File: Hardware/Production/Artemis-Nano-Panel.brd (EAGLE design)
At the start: 120.7 x 75.7 mm, 768 parts, among them J10 USB-C, J11 CORTEX_DEBUG, J21 USB-C, J22 CORTEX_DEBUG, J32 USB-C, J33 CORTEX_DEBUG, J43 USB-C, J44 CORTEX_DEBUG, J54 USB-C, J55 CORTEX_DEBUG, J65 USB-C, J66 CORTEX_DEBUG, U1 MCP73831, U10 3.3V, U11 ARTEMIS_MODULESMD, U12 CH340E_MSOP10, U13 MCP73831, U14 3.3V, U15 ARTEMIS_MODULESMD, U16 CH340E_MSOP10, U17 MCP73831, U18 3.3V, U19 ARTEMIS_MODULESMD, U2 MCP73831, U20 CH340E_MSOP10, U21 MCP73831, U22 3.3V, U23 ARTEMIS_MODULESMD, U24 CH340E_MSOP10, U3 3.3V, U4 ARTEMIS_MODULESMD, U5 3.3V, U6 CH340E_MSOP10, U7 ARTEMIS_MODULESMD, U8 CH340E_MSOP10, U9 MCP73831, Y1 32.768kHz, Y2 32.768kHz, Y3 32.768kHz, Y4 32.768kHz, Y5 32.768kHz, Y6 32.768kHz

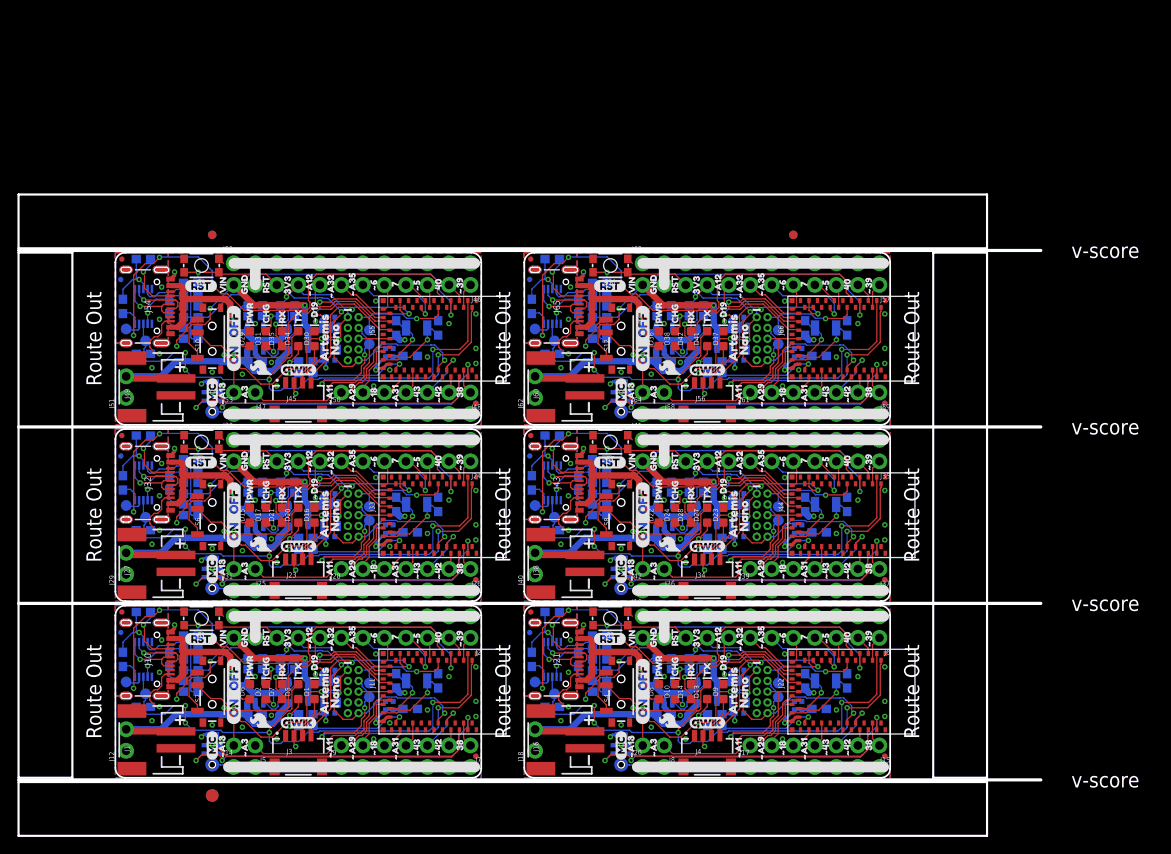
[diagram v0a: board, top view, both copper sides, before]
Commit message: Fixed TX/RX LED label swap
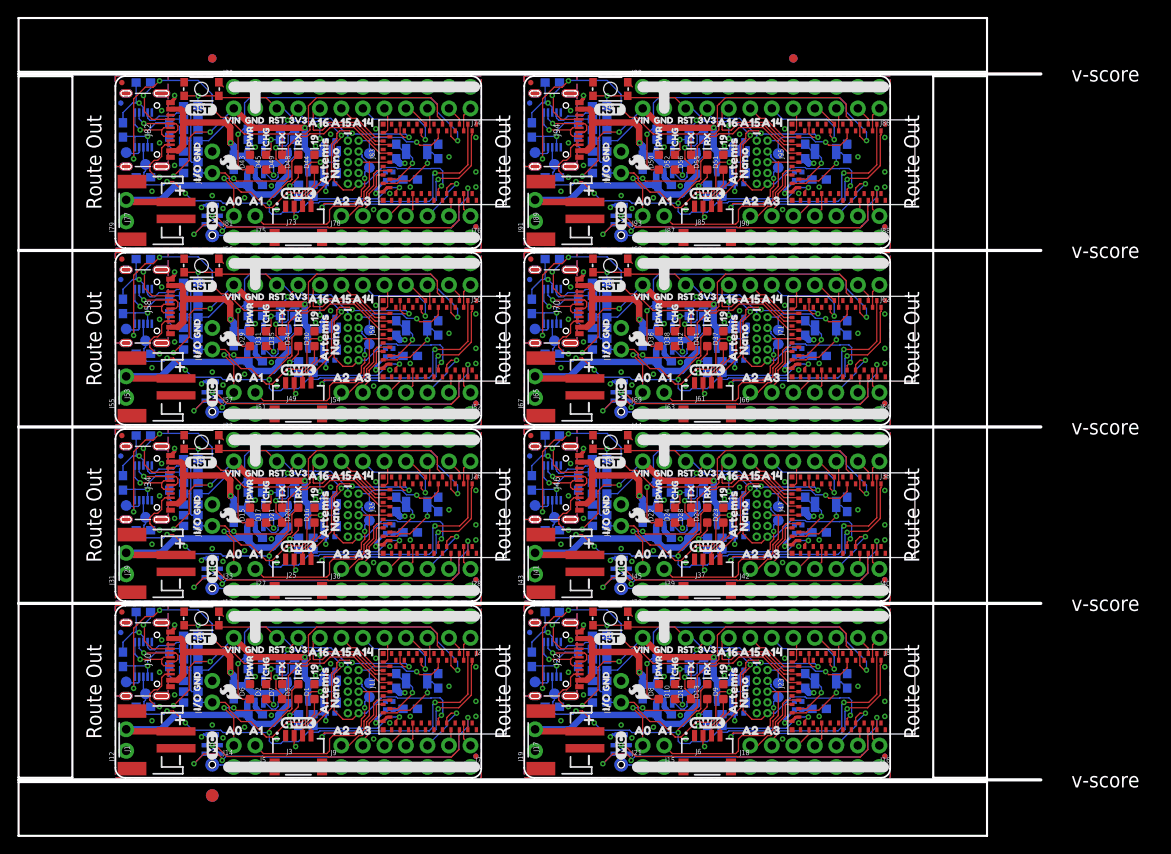
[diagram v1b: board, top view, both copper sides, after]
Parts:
- removed S10, S12: (no value), SparkFun-Switches:SWITCH_SPST_SMD_A
- removed S11, S9: RESET, SparkFun-Switches:TACTILE_SWITCH_SMD_4.6X2.8MM
- added C100, C113, C115, C98: 0.1uF, SparkFun-Capacitors:0603
- added C101, C116: 2.2uF, SparkFun-Capacitors:0603
- added C102, C117: 10uF, SparkFun-Capacitors:0603
- added C103, C108, C109, C118, C93, C94: 1.0uF, SparkFun-Capacitors:0402-TIGHT
- added C104, C119: 1nF, SparkFun-Capacitors:0603
- added C105, C114, C120, C99: 0.1uF, SparkFun-Capacitors:0402-TIGHT
- added C106, C107, C91, C92: 4.7uF, SparkFun-Capacitors:0603
- added C110, C111, C95, C96: 15pF, SparkFun-Capacitors:0603
- added C112, C97: 10nF, SparkFun-Capacitors:0603
- added D43, D50: RED, SparkFun-LED:LED-0603
- added D44, D51: BLUE, SparkFun-LED:LED-0603
- added D45, D48, D52, D55: Yellow, SparkFun-LED:LED-0603
- added D46, D47, D53, D54: 1A/23V/620mV, SparkFun-DiscreteSemi:SOD-323
- added D49, D56: GREEN, SparkFun-LED:LED-0603
- added E7, E8: SPH0641LM4H, SparkFun-Sensors:SPH0641LM4H-1_MICROPHONE
- added FD25, FD26, FD27, FD28, FD29, FD30, FD31, FD32: FIDUCIALUFIDUCIAL, SparkFun-Aesthetics:FIDUCIAL-MICRO
- added FRAME7, FRAME8: FRAME-LETTERNO_PACKAGE, SparkFun-Aesthetics:DUMMY
- added J67, J69, J72, J75, J79, J81, J84, J87, J91, J93, J96: (no value), SparkFun-Connectors:1X02_NO_SILK
- added J68, J74, J80, J86, J92: (no value), SparkFun-Connectors:1X12_NO_SILK
- added J70, J82, J94: USB-C, SparkFun-Connectors:USB-C-16P
- added J71, J83, J95: CORTEX_DEBUG, SparkFun-Connectors:2X5-PTH-1.27MM-NO_SILK
- added J73, J85: (no value), SparkFun-Connectors:JST04_1MM_RA
- added J76, J78, J88, J90: (no value), SparkFun-Connectors:1X07_NO_SILK
- added J77, J89: (no value), SparkFun-Connectors:JST-2-SMD
- added LOGO13, LOGO14, LOGO15, LOGO16: SFE_LOGO_FLAME.1_INCH, SparkFun-Aesthetics:SFE_LOGO_FLAME_.1
- added R67, R68, R79, R80, R91, R92: 5.1k, SparkFun-Resistors:0603
- added R69, R71, R81, R83, R93, R95: 100k, SparkFun-Resistors:0603
- added R70, R72, R82, R84, R94, R96: 10k, SparkFun-Resistors:0603
- added R73, R74, R76, R85, R86, R88: 1k, SparkFun-Resistors:0603
- added R75, R87: 2.0k, SparkFun-Resistors:0603
- added R77, R78, R89, R90: 4.7k, SparkFun-Resistors:0603
- added TP25, TP26, TP29, TP30: TEST-POINT3X5, SparkFun-Connectors:PAD.03X.05
- added TP27, TP28, TP31, TP32: (no value), SparkFun-Connectors:PAD.03X.05
- added U$385, U$445: (no value), SparkFun-Aesthetics:PRODUCTION_INSTRUCTIONS
- added U$386, U$408, U$446, U$468: (no value), buzzard_labels (16):A00
- added U$387, U$447: (no value), buzzard_labels:46
- added U$388, U$448: (no value), buzzard_labels:68
- added U$389, U$449: (no value), buzzard_labels:79
- added U$390, U$450: (no value), buzzard_labels:810
- added U$391, U$409, U$451, U$469: (no value), buzzard_labels:A10
- added U$392, U$407, U$452, U$467: (no value), buzzard_labels:A21
- added U$393, U$406, U$453, U$466: (no value), buzzard_labels:A32
- added U$394, U$454: (no value), buzzard_labels (1):90
- added U$395, U$455: (no value), buzzard_labels (1):101
- added U$396, U$456: (no value), buzzard_labels (1):112
- added U$397, U$457: (no value), buzzard_labels (1):123
- added U$398, U$458: (no value), buzzard_labels (1):134
- added U$399, U$410, U$459, U$470: (no value), buzzard_labels (1):A145
- added U$400, U$411, U$460, U$471: (no value), buzzard_labels (1):A156
- added U$401, U$412, U$461, U$472: (no value), buzzard_labels (1):A167
- added U$402, U$462: (no value), buzzard_labels (2):SCL30
- added U$403, U$463: (no value), buzzard_labels (2):SDA31
- added U$404, U$464: (no value), buzzard_labels (2):TX12
- added U$405, U$465: (no value), buzzard_labels:A57
- added U$413, U$473: (no value), buzzard_labels (3):RX10
- added U$414, U$474: (no value), buzzard_labels (5):17#SDA21
- added U$415, U$475: (no value), buzzard_labels (5):18#SCL20
- added U$416, U$476: (no value), buzzard_labels (6):191
- added U$417, U$419, U$477, U$479: (no value), buzzard_labels (7):I#O3
- added U$418, U$420, U$424, U$431, U$478, U$480: (no value), buzzard_labels:GND17
- added U$421: (no value), buzzard_labels:CHG26
- added U$422: (no value), buzzard_labels:PWR27
- added U$423: (no value), qwiic#logo#jpg:QWIIC#LOGO#JPG
- added U$425, U$433: (no value), buzzard_labels:VIN19
- added U$426, U$432: (no value), buzzard_labels:RST19
- added U$427, U$434: (no value), buzzard_labels:3V316
- added U$428: (no value), buzzard_labels:RST1
- added U$429: (no value), buzzard_labels (10):RX23
- added U$430: (no value), buzzard_labels (10):TX22
- added U$435, U$441: (no value), buzzard_labels (11):ARTEMIS6
- added U$436: (no value), buzzard_labels (11):MIC0
- added U$437: (no value), buzzard_labels (11):MISO5
- added U$438: (no value), buzzard_labels (11):MOSI4
- added U$439, U$442: (no value), buzzard_labels (11):NANO7
- added U$440: (no value), buzzard_labels (11):SCK3
- added U$443: (no value), buzzard_labels (16):GND2
- added U$444: (no value), buzzard_labels (17):____GND____2
- added U25, U29: MCP73831, SparkFun-IC-Power:SOT23-5
- added U26, U30: 3.3V, SparkFun-IC-Power:SOT23-5
- added U27, U31: ARTEMIS_MODULESMD, Testing:ARTEMIS_FP
- added U28, U32: CH340E_MSOP10, SparkFun-IC-Comms:MSOP10
- added Y7, Y8: 32.768kHz, SparkFun-Clocks:CRYSTAL-SMD-3.2X1.5MM
- J15, J39, J48: device SparkFun-Connectors:1X07_NO_SILK -> SparkFun-Connectors:1X02_NO_SILK
- J16: device SparkFun-Connectors:JST-2-SMD -> SparkFun-Connectors:1X07_NO_SILK
- J17: device SparkFun-Connectors:1X07_NO_SILK -> SparkFun-Connectors:JST-2-SMD
- J18, J40, J42, J64: device SparkFun-Connectors:1X02_NO_SILK -> SparkFun-Connectors:1X07_NO_SILK
- J19, J24, J57, J63: device SparkFun-Connectors:1X12_NO_SILK -> SparkFun-Connectors:1X02_NO_SILK
- J20, J62, J8: device SparkFun-Connectors:1X02_NO_SILK -> SparkFun-Connectors:1X12_NO_SILK
- J21, J43: value USB-C -> (none); device SparkFun-Connectors:USB-C-16P -> SparkFun-Connectors:1X02_NO_SILK
- J22: value CORTEX_DEBUG -> USB-C; device SparkFun-Connectors:2X5-PTH-1.27MM-NO_SILK -> SparkFun-Connectors:USB-C-16P
- J23: value (none) -> CORTEX_DEBUG; device SparkFun-Connectors:JST04_1MM_RA -> SparkFun-Connectors:2X5-PTH-1.27MM-NO_SILK
- J25: device SparkFun-Connectors:1X02_NO_SILK -> SparkFun-Connectors:JST04_1MM_RA
- J26, J50: device SparkFun-Connectors:1X07_NO_SILK -> SparkFun-Connectors:1X12_NO_SILK
- J27, J60: device SparkFun-Connectors:JST-2-SMD -> SparkFun-Connectors:1X02_NO_SILK
- J29, J53: device SparkFun-Connectors:1X02_NO_SILK -> SparkFun-Connectors:JST-2-SMD
- J30, J52: device SparkFun-Connectors:1X12_NO_SILK -> SparkFun-Connectors:1X07_NO_SILK
- J32: value USB-C -> (none); device SparkFun-Connectors:USB-C-16P -> SparkFun-Connectors:1X12_NO_SILK
- J33, J55: value CORTEX_DEBUG -> (none); device SparkFun-Connectors:2X5-PTH-1.27MM-NO_SILK -> SparkFun-Connectors:1X02_NO_SILK
- J34: value (none) -> USB-C; device SparkFun-Connectors:JST04_1MM_RA -> SparkFun-Connectors:USB-C-16P
- J35: value (none) -> CORTEX_DEBUG; device SparkFun-Connectors:1X12_NO_SILK -> SparkFun-Connectors:2X5-PTH-1.27MM-NO_SILK
- J37, J61: device SparkFun-Connectors:1X07_NO_SILK -> SparkFun-Connectors:JST04_1MM_RA
- J38: device SparkFun-Connectors:JST-2-SMD -> SparkFun-Connectors:1X12_NO_SILK
- J4, J45: device SparkFun-Connectors:JST04_1MM_RA -> SparkFun-Connectors:1X02_NO_SILK
- J41: device SparkFun-Connectors:1X12_NO_SILK -> SparkFun-Connectors:JST-2-SMD
- J44: value CORTEX_DEBUG -> (none); device SparkFun-Connectors:2X5-PTH-1.27MM-NO_SILK -> SparkFun-Connectors:1X12_NO_SILK
- J46: value (none) -> USB-C; device SparkFun-Connectors:1X12_NO_SILK -> SparkFun-Connectors:USB-C-16P
- J47: value (none) -> CORTEX_DEBUG; device SparkFun-Connectors:1X02_NO_SILK -> SparkFun-Connectors:2X5-PTH-1.27MM-NO_SILK
- J49: device SparkFun-Connectors:JST-2-SMD -> SparkFun-Connectors:JST04_1MM_RA
- J54: value USB-C -> (none); device SparkFun-Connectors:USB-C-16P -> SparkFun-Connectors:1X07_NO_SILK
- J56: device SparkFun-Connectors:JST04_1MM_RA -> SparkFun-Connectors:1X12_NO_SILK
- J58: value (none) -> USB-C; device SparkFun-Connectors:1X02_NO_SILK -> SparkFun-Connectors:USB-C-16P
- J59: value (none) -> CORTEX_DEBUG; device SparkFun-Connectors:1X07_NO_SILK -> SparkFun-Connectors:2X5-PTH-1.27MM-NO_SILK
- J6: device SparkFun-Connectors:1X12_NO_SILK -> SparkFun-Connectors:JST04_1MM_RA
- J65: value USB-C -> (none); device SparkFun-Connectors:USB-C-16P -> SparkFun-Connectors:JST-2-SMD
- J66: value CORTEX_DEBUG -> (none); device SparkFun-Connectors:2X5-PTH-1.27MM-NO_SILK -> SparkFun-Connectors:1X07_NO_SILK
- R1, R24, R34, R46, R48: value 1k -> 10k
- R18, R29, R30, R41: value 5.1k -> 4.7k
- R20, R31, R44, R55: value 100k -> 5.1k
- R21: value 10k -> 100k
- R22: value 100k -> 10k
- R23, R35, R45, R57, R59: value 1k -> 100k
- R25, R4: value 2.0k -> 1k
- R27, R39: value 4.7k -> 2.0k
- R28, R38, R49, R50, R61, R8: value 4.7k -> 1k
- R32, R43: value 10k -> 5.1k
- R36, R58: value 2.0k -> 10k
- R40, R52, R62: value 5.1k -> 1k
- R42, R53, R66: value 100k -> 4.7k
- R47: value 2.0k -> 100k
- R51, R63: value 5.1k -> 2.0k
- R54, R65: value 10k -> 4.7k
- R56: value 1k -> 5.1k
- R60: value 4.7k -> 10k
- R64: value 100k -> 1k
- R7: value 1k -> 2.0k
- S2, S4, S6, S8: value (none) -> RESET; device SparkFun-Switches:SWITCH_SPST_SMD_A -> SparkFun-Switches:TACTILE_SWITCH_SMD_4.6X2.8MM
- U$10: device buzzard_labels (11):#A312 -> buzzard_labels:A57
- U$100: device buzzard_labels (10):TX22 -> buzzard_labels (1):A156
- U$101: device buzzard_labels (10):#A120 -> buzzard_labels (1):A167
- U$102: device buzzard_labels:GND17 -> buzzard_labels (2):SCL30
- U$103: device buzzard_labels:RST19 -> buzzard_labels (2):SDA31
- U$104: device buzzard_labels:VIN19 -> buzzard_labels (2):TX12
- U$105: device buzzard_labels:3V316 -> buzzard_labels:A57
- U$106: device buzzard_labels (8):#A112 -> buzzard_labels:A32
- U$107: device buzzard_labels (10):3812 -> buzzard_labels:A21
- U$108, U$9: device buzzard_labels (11):#A312 -> buzzard_labels (16):A00
- U$109: device buzzard_labels (11):#A312 -> buzzard_labels:A10
- U$11: device buzzard_labels (11):#A321 -> buzzard_labels (2):SCL30
- U$110, U$12: device buzzard_labels (11):#A321 -> buzzard_labels (1):A145
- U$111: device buzzard_labels (11):#A321 -> buzzard_labels (1):A156
- U$112: device buzzard_labels (11):ARTEMIS6 -> buzzard_labels (1):A167
- U$113: device buzzard_labels (11):MIC0 -> buzzard_labels (3):RX10
- U$114: device buzzard_labels (11):MISO5 -> buzzard_labels (5):17#SDA21
- U$115: device buzzard_labels (11):MOSI4 -> buzzard_labels (5):18#SCL20
- U$116: device buzzard_labels (11):NANO7 -> buzzard_labels (6):191
- U$117: device buzzard_labels (11):SCK3 -> buzzard_labels (7):I#O3
- U$118: device buzzard_labels (10):#510 -> buzzard_labels:GND17
- U$119: device buzzard_labels (10):78 -> buzzard_labels (7):I#O3
- U$120, U$184: device buzzard_labels (10):#66 -> buzzard_labels:GND17
- U$121: device buzzard_labels (11):ARTEMIS6 -> buzzard_labels:CHG26
- U$122: device buzzard_labels (11):NANO7 -> buzzard_labels:PWR27
- U$123: device buzzard_labels (14):#D190 -> qwiic#logo#jpg:QWIIC#LOGO#JPG
- U$124: device buzzard_labels (16):#25#SDA21 -> buzzard_labels:GND17
- U$125, U$253: device buzzard_labels (16):#27#SCL20 -> buzzard_labels:VIN19
- U$126: device buzzard_labels (16):GND2 -> buzzard_labels:RST19
- U$127: device buzzard_labels (17):____GND____2 -> buzzard_labels:3V316
- U$128: device SparkFun-Aesthetics:PRODUCTION_INSTRUCTIONS -> buzzard_labels:RST1
- U$129: device buzzard_labels:CHG26 -> buzzard_labels (10):RX23
- U$130: device buzzard_labels:PWR27 -> buzzard_labels (10):TX22
- U$131: device qwiic#logo#jpg:QWIIC#LOGO#JPG -> buzzard_labels:GND17
- U$132: device buzzard_labels:GND17 -> buzzard_labels:RST19
- U$134: device buzzard_labels:RST19 -> buzzard_labels:3V316
- U$135: device buzzard_labels:3V316 -> buzzard_labels (11):ARTEMIS6
- U$136: device buzzard_labels:RST1 -> buzzard_labels (11):MIC0
- U$137: device buzzard_labels:ON1 -> buzzard_labels (11):MISO5
- U$138: device buzzard_labels:OFF2 -> buzzard_labels (11):MOSI4
- U$139: device buzzard_labels (8):#A112 -> buzzard_labels (11):NANO7
- U$140: device buzzard_labels (10):#39#TX13 -> buzzard_labels (11):SCK3
- U$141: device buzzard_labels (10):#42#SCL314 -> buzzard_labels (11):ARTEMIS6
- U$142: device buzzard_labels (10):#43#SDA316 -> buzzard_labels (11):NANO7
- U$143: device buzzard_labels (10):#66 -> buzzard_labels (16):GND2
- U$144: device buzzard_labels (10):#394 -> buzzard_labels (17):____GND____2
- U$145: device buzzard_labels (10):#510 -> SparkFun-Aesthetics:PRODUCTION_INSTRUCTIONS
- U$146: device buzzard_labels (10):#1818 -> buzzard_labels (16):A00
- U$147: device buzzard_labels (10):#1818 -> buzzard_labels:46
- U$148: device buzzard_labels (10):#4213 -> buzzard_labels:68
- U$149: device buzzard_labels (10):#4315 -> buzzard_labels:79
- U$150: device buzzard_labels (10):#A120 -> buzzard_labels:810
- U$151: device buzzard_labels (10):#A320 -> buzzard_labels:A10
- U$152: device buzzard_labels (10):#A320 -> buzzard_labels:A21
- U$153, U$346: device buzzard_labels (10):#A351 -> buzzard_labels:A32
- U$154: device buzzard_labels (10):#A351 -> buzzard_labels (1):90
- U$155: device buzzard_labels (10):#A1321 -> buzzard_labels (1):101
- U$156: device buzzard_labels (10):#A1321 -> buzzard_labels (1):112
- U$157: device buzzard_labels (10):#A2919 -> buzzard_labels (1):123
- U$158: device buzzard_labels (10):#A2919 -> buzzard_labels (1):134
- U$159: device buzzard_labels (10):40#RX12 -> buzzard_labels (1):A145
- U$160: device buzzard_labels (10):78 -> buzzard_labels (1):A156
- U$161: device buzzard_labels (10):405 -> buzzard_labels (1):A167
- U$162: device buzzard_labels (10):3812 -> buzzard_labels (2):SCL30
- U$163: device buzzard_labels (10):RX23 -> buzzard_labels (2):SDA31
- U$164: device buzzard_labels (10):TX22 -> buzzard_labels (2):TX12
- U$165: device buzzard_labels (10):#A120 -> buzzard_labels:A57
- U$166: device buzzard_labels:GND17 -> buzzard_labels:A32
- U$167: device buzzard_labels:RST19 -> buzzard_labels:A21
- U$168: device buzzard_labels:VIN19 -> buzzard_labels (16):A00
- U$169: device buzzard_labels:3V316 -> buzzard_labels:A10
- U$170: device buzzard_labels (8):#A112 -> buzzard_labels (1):A145
- U$171: device buzzard_labels (10):3812 -> buzzard_labels (1):A156
- U$172: device buzzard_labels (11):#A312 -> buzzard_labels (1):A167
- U$173: device buzzard_labels (11):#A312 -> buzzard_labels (3):RX10
- U$174: device buzzard_labels (11):#A321 -> buzzard_labels (5):17#SDA21
- U$175: device buzzard_labels (11):#A321 -> buzzard_labels (5):18#SCL20
- U$176: device buzzard_labels (11):ARTEMIS6 -> buzzard_labels (6):191
- U$177: device buzzard_labels (11):MIC0 -> buzzard_labels (7):I#O3
- U$178: device buzzard_labels (11):MISO5 -> buzzard_labels:GND17
- U$179: device buzzard_labels (11):MOSI4 -> buzzard_labels (7):I#O3
- U$180, U$244: device buzzard_labels (11):NANO7 -> buzzard_labels:GND17
- U$181: device buzzard_labels (11):SCK3 -> buzzard_labels:CHG26
- U$182: device buzzard_labels (10):#510 -> buzzard_labels:PWR27
- U$183: device buzzard_labels (10):78 -> qwiic#logo#jpg:QWIIC#LOGO#JPG
- U$185, U$313: device buzzard_labels (11):ARTEMIS6 -> buzzard_labels:VIN19
- U$186, U$372: device buzzard_labels (11):NANO7 -> buzzard_labels:RST19
- U$187: device buzzard_labels (14):#D190 -> buzzard_labels:3V316
- U$188: device buzzard_labels (16):#25#SDA21 -> buzzard_labels:RST1
- U$189: device buzzard_labels (16):#27#SCL20 -> buzzard_labels (10):RX23
- U$19, U$273: device buzzard_labels (10):#510 -> buzzard_labels:A32
- U$190: device buzzard_labels (16):GND2 -> buzzard_labels (10):TX22
- U$191: device buzzard_labels (17):____GND____2 -> buzzard_labels:GND17
- U$192: device SparkFun-Aesthetics:PRODUCTION_INSTRUCTIONS -> buzzard_labels:RST19
- U$193: device buzzard_labels:CHG26 -> buzzard_labels:VIN19
- U$194: device buzzard_labels:PWR27 -> buzzard_labels:3V316
- U$195: device qwiic#logo#jpg:QWIIC#LOGO#JPG -> buzzard_labels (11):ARTEMIS6
- U$196: device buzzard_labels:GND17 -> buzzard_labels (11):MIC0
- U$197: device buzzard_labels:VIN19 -> buzzard_labels (11):MISO5
- U$198: device buzzard_labels:RST19 -> buzzard_labels (11):MOSI4
- U$199: device buzzard_labels:3V316 -> buzzard_labels (11):NANO7
- U$20, U$288: device buzzard_labels (10):78 -> buzzard_labels (16):A00
- U$200: device buzzard_labels:RST1 -> buzzard_labels (11):SCK3
- U$201: device buzzard_labels:ON1 -> buzzard_labels (11):ARTEMIS6
- U$202: device buzzard_labels:OFF2 -> buzzard_labels (11):NANO7
- U$203: device buzzard_labels (8):#A112 -> buzzard_labels (16):GND2
- U$204: device buzzard_labels (10):#39#TX13 -> buzzard_labels (17):____GND____2
- U$205: device buzzard_labels (10):#42#SCL314 -> SparkFun-Aesthetics:PRODUCTION_INSTRUCTIONS
- U$206: device buzzard_labels (10):#43#SDA316 -> buzzard_labels (16):A00
- U$207: device buzzard_labels (10):#66 -> buzzard_labels:46
- U$208: device buzzard_labels (10):#394 -> buzzard_labels:68
- U$209: device buzzard_labels (10):#510 -> buzzard_labels:79
- U$21: device buzzard_labels (10):#66 -> buzzard_labels:A21
- U$210: device buzzard_labels (10):#1818 -> buzzard_labels:810
- U$211: device buzzard_labels (10):#1818 -> buzzard_labels:A10
- U$212: device buzzard_labels (10):#4213 -> buzzard_labels:A21
- U$213: device buzzard_labels (10):#4315 -> buzzard_labels:A32
- U$214: device buzzard_labels (10):#A120 -> buzzard_labels (1):90
- U$215: device buzzard_labels (10):#A320 -> buzzard_labels (1):101
- U$216: device buzzard_labels (10):#A320 -> buzzard_labels (1):112
- U$217: device buzzard_labels (10):#A351 -> buzzard_labels (1):123
- U$218: device buzzard_labels (10):#A351 -> buzzard_labels (1):134
- U$219: device buzzard_labels (10):#A1321 -> buzzard_labels (1):A145
- U$220: device buzzard_labels (10):#A1321 -> buzzard_labels (1):A156
- U$221: device buzzard_labels (10):#A2919 -> buzzard_labels (1):A167
- U$222: device buzzard_labels (10):#A2919 -> buzzard_labels (2):SCL30
- U$223: device buzzard_labels (10):40#RX12 -> buzzard_labels (2):SDA31
- U$224: device buzzard_labels (10):78 -> buzzard_labels (2):TX12
- U$225: device buzzard_labels (10):405 -> buzzard_labels:A57
- U$226: device buzzard_labels (10):3812 -> buzzard_labels:A32
- U$227: device buzzard_labels (10):RX23 -> buzzard_labels:A21
- U$228: device buzzard_labels (10):TX22 -> buzzard_labels (16):A00
- U$229: device buzzard_labels (10):#A120 -> buzzard_labels:A10
- U$23: device buzzard_labels (14):#D190 -> buzzard_labels (7):I#O3
- U$230: device buzzard_labels:GND17 -> buzzard_labels (1):A145
- U$231: device buzzard_labels:RST19 -> buzzard_labels (1):A156
- U$232: device buzzard_labels:VIN19 -> buzzard_labels (1):A167
- U$233: device buzzard_labels:3V316 -> buzzard_labels (3):RX10
- U$234: device buzzard_labels (8):#A112 -> buzzard_labels (5):17#SDA21
- U$235: device buzzard_labels (10):3812 -> buzzard_labels (5):18#SCL20
- U$236: device buzzard_labels (11):#A312 -> buzzard_labels (6):191
- U$237: device buzzard_labels (11):#A312 -> buzzard_labels (7):I#O3
- U$238: device buzzard_labels (11):#A321 -> buzzard_labels:GND17
- U$239: device buzzard_labels (11):#A321 -> buzzard_labels (7):I#O3
- U$240, U$304: device buzzard_labels (11):ARTEMIS6 -> buzzard_labels:GND17
- U$241: device buzzard_labels (11):MIC0 -> buzzard_labels:CHG26
- U$242: device buzzard_labels (11):MISO5 -> buzzard_labels:PWR27
- U$243: device buzzard_labels (11):MOSI4 -> qwiic#logo#jpg:QWIIC#LOGO#JPG
- U$245, U$373: device buzzard_labels (11):SCK3 -> buzzard_labels:VIN19
- U$246: device buzzard_labels (10):#510 -> buzzard_labels:RST19
- U$247: device buzzard_labels (10):78 -> buzzard_labels:3V316
- U$248: device buzzard_labels (10):#66 -> buzzard_labels:RST1
- U$249: device buzzard_labels (11):ARTEMIS6 -> buzzard_labels (10):RX23
- U$250: device buzzard_labels (11):NANO7 -> buzzard_labels (10):TX22
- U$251: device buzzard_labels (14):#D190 -> buzzard_labels:GND17
- U$252: device buzzard_labels (16):#25#SDA21 -> buzzard_labels:RST19
- U$254: device buzzard_labels (16):GND2 -> buzzard_labels:3V316
- U$255: device buzzard_labels (17):____GND____2 -> buzzard_labels (11):ARTEMIS6
- U$256: device SparkFun-Aesthetics:PRODUCTION_INSTRUCTIONS -> buzzard_labels (11):MIC0
- U$257: device buzzard_labels:CHG26 -> buzzard_labels (11):MISO5
- U$258: device buzzard_labels:PWR27 -> buzzard_labels (11):MOSI4
- U$259: device qwiic#logo#jpg:QWIIC#LOGO#JPG -> buzzard_labels (11):NANO7
- U$26: device buzzard_labels (16):#25#SDA21 -> buzzard_labels (6):191
- U$260: device buzzard_labels:GND17 -> buzzard_labels (11):SCK3
- U$261: device buzzard_labels:VIN19 -> buzzard_labels (11):ARTEMIS6
- U$262: device buzzard_labels:RST19 -> buzzard_labels (11):NANO7
- U$263: device buzzard_labels:3V316 -> buzzard_labels (16):GND2
- U$264: device buzzard_labels:RST1 -> buzzard_labels (17):____GND____2
- U$265: device buzzard_labels:ON1 -> SparkFun-Aesthetics:PRODUCTION_INSTRUCTIONS
- U$266: device buzzard_labels:OFF2 -> buzzard_labels (16):A00
- U$267: device buzzard_labels (8):#A112 -> buzzard_labels:46
- U$268: device buzzard_labels (10):#39#TX13 -> buzzard_labels:68
- U$269: device buzzard_labels (10):#42#SCL314 -> buzzard_labels:79
- U$270: device buzzard_labels (10):#43#SDA316 -> buzzard_labels:810
- U$271: device buzzard_labels (10):#66 -> buzzard_labels:A10
- U$272: device buzzard_labels (10):#394 -> buzzard_labels:A21
- U$274: device buzzard_labels (10):#1818 -> buzzard_labels (1):90
- U$275: device buzzard_labels (10):#1818 -> buzzard_labels (1):101
- U$276: device buzzard_labels (10):#4213 -> buzzard_labels (1):112
- U$277: device buzzard_labels (10):#4315 -> buzzard_labels (1):123
- U$278: device buzzard_labels (10):#A120 -> buzzard_labels (1):134
- U$279: device buzzard_labels (10):#A320 -> buzzard_labels (1):A145
- U$28: device buzzard_labels (10):#A120 -> buzzard_labels (1):A156
- U$280: device buzzard_labels (10):#A320 -> buzzard_labels (1):A156
- U$281: device buzzard_labels (10):#A351 -> buzzard_labels (1):A167
- U$282: device buzzard_labels (10):#A351 -> buzzard_labels (2):SCL30
- U$283: device buzzard_labels (10):#A1321 -> buzzard_labels (2):SDA31
- U$284: device buzzard_labels (10):#A1321 -> buzzard_labels (2):TX12
- U$285: device buzzard_labels (10):#A2919 -> buzzard_labels:A57
- U$286, U$93: device buzzard_labels (10):#A2919 -> buzzard_labels:A32
- U$287: device buzzard_labels (10):40#RX12 -> buzzard_labels:A21
- U$289: device buzzard_labels (10):405 -> buzzard_labels:A10
- U$29: device buzzard_labels (16):#27#SCL20 -> buzzard_labels:GND17
- U$290: device buzzard_labels (10):3812 -> buzzard_labels (1):A145
- U$291: device buzzard_labels (10):RX23 -> buzzard_labels (1):A156
- U$292: device buzzard_labels (10):TX22 -> buzzard_labels (1):A167
- U$293: device buzzard_labels (10):#A120 -> buzzard_labels (3):RX10
- U$294: device buzzard_labels:GND17 -> buzzard_labels (5):17#SDA21
- U$295: device buzzard_labels:RST19 -> buzzard_labels (5):18#SCL20
- U$296: device buzzard_labels:VIN19 -> buzzard_labels (6):191
- U$297: device buzzard_labels:3V316 -> buzzard_labels (7):I#O3
- U$298: device buzzard_labels (8):#A112 -> buzzard_labels:GND17
- U$299: device buzzard_labels (10):3812 -> buzzard_labels (7):I#O3
- U$300, U$364: device buzzard_labels (11):#A312 -> buzzard_labels:GND17
- U$301: device buzzard_labels (11):#A312 -> buzzard_labels:CHG26
- U$302: device buzzard_labels (11):#A321 -> buzzard_labels:PWR27
- U$303: device buzzard_labels (11):#A321 -> qwiic#logo#jpg:QWIIC#LOGO#JPG
- U$305: device buzzard_labels (11):MIC0 -> buzzard_labels:VIN19
- U$306: device buzzard_labels (11):MISO5 -> buzzard_labels:RST19
- U$307: device buzzard_labels (11):MOSI4 -> buzzard_labels:3V316
- U$308: device buzzard_labels (11):NANO7 -> buzzard_labels:RST1
- U$309: device buzzard_labels (11):SCK3 -> buzzard_labels (10):RX23
- U$31: device buzzard_labels (10):3812 -> buzzard_labels (2):SDA31
- U$310: device buzzard_labels (10):#510 -> buzzard_labels (10):TX22
- U$311: device buzzard_labels (10):78 -> buzzard_labels:GND17
- U$312: device buzzard_labels (10):#66 -> buzzard_labels:RST19
- U$314: device buzzard_labels (11):NANO7 -> buzzard_labels:3V316
- U$315: device buzzard_labels (14):#D190 -> buzzard_labels (11):ARTEMIS6
- U$316: device buzzard_labels (16):#25#SDA21 -> buzzard_labels (11):MIC0
- U$317: device buzzard_labels (16):#27#SCL20 -> buzzard_labels (11):MISO5
- U$318: device buzzard_labels (16):GND2 -> buzzard_labels (11):MOSI4
- U$319: device buzzard_labels (17):____GND____2 -> buzzard_labels (11):NANO7
- U$32: device buzzard_labels:CHG26 -> buzzard_labels:46
- U$320: device SparkFun-Aesthetics:PRODUCTION_INSTRUCTIONS -> buzzard_labels (11):SCK3
- U$321: device buzzard_labels:CHG26 -> buzzard_labels (11):ARTEMIS6
- U$322: device buzzard_labels:PWR27 -> buzzard_labels (11):NANO7
- U$323: device qwiic#logo#jpg:QWIIC#LOGO#JPG -> buzzard_labels (16):GND2
- U$324: device buzzard_labels:GND17 -> buzzard_labels (17):____GND____2
- U$325: device buzzard_labels:VIN19 -> SparkFun-Aesthetics:PRODUCTION_INSTRUCTIONS
- U$326: device buzzard_labels:RST19 -> buzzard_labels (16):A00
- U$327: device buzzard_labels:3V316 -> buzzard_labels:46
- U$328: device buzzard_labels:RST1 -> buzzard_labels:68
- U$329: device buzzard_labels:ON1 -> buzzard_labels:79
- U$330: device buzzard_labels:OFF2 -> buzzard_labels:810
- U$331: device buzzard_labels (8):#A112 -> buzzard_labels:A10
- U$332: device buzzard_labels (10):#39#TX13 -> buzzard_labels:A21
- U$333: device buzzard_labels (10):#42#SCL314 -> buzzard_labels:A32
- U$334: device buzzard_labels (10):#43#SDA316 -> buzzard_labels (1):90
- U$335: device buzzard_labels (10):#66 -> buzzard_labels (1):101
- U$336: device buzzard_labels (10):#394 -> buzzard_labels (1):112
- U$337: device buzzard_labels (10):#510 -> buzzard_labels (1):123
- U$338: device buzzard_labels (10):#1818 -> buzzard_labels (1):134
- U$339: device buzzard_labels (10):#1818 -> buzzard_labels (1):A145
- U$34: device buzzard_labels:PWR27 -> buzzard_labels:A10
- U$340: device buzzard_labels (10):#4213 -> buzzard_labels (1):A156
- U$341: device buzzard_labels (10):#4315 -> buzzard_labels (1):A167
- U$342: device buzzard_labels (10):#A120 -> buzzard_labels (2):SCL30
- U$343: device buzzard_labels (10):#A320 -> buzzard_labels (2):SDA31
- U$344: device buzzard_labels (10):#A320 -> buzzard_labels (2):TX12
- U$345: device buzzard_labels (10):#A351 -> buzzard_labels:A57
- U$347, U$92: device buzzard_labels (10):#A1321 -> buzzard_labels:A21
- U$348: device buzzard_labels (10):#A1321 -> buzzard_labels (16):A00
- U$349: device buzzard_labels (10):#A2919 -> buzzard_labels:A10
- U$35: device qwiic#logo#jpg:QWIIC#LOGO#JPG -> buzzard_labels:68
- U$350: device buzzard_labels (10):#A2919 -> buzzard_labels (1):A145
- U$351: device buzzard_labels (10):40#RX12 -> buzzard_labels (1):A156
- U$352: device buzzard_labels (10):78 -> buzzard_labels (1):A167
- U$353: device buzzard_labels (10):405 -> buzzard_labels (3):RX10
- U$354: device buzzard_labels (10):3812 -> buzzard_labels (5):17#SDA21
- U$355: device buzzard_labels (10):RX23 -> buzzard_labels (5):18#SCL20
- U$356: device buzzard_labels (10):TX22 -> buzzard_labels (6):191
- U$357: device buzzard_labels (10):#A120 -> buzzard_labels (7):I#O3
- U$359: device buzzard_labels:RST19 -> buzzard_labels (7):I#O3
- U$36: device buzzard_labels:GND17 -> buzzard_labels:79
- U$360: device buzzard_labels:VIN19 -> buzzard_labels:GND17
- U$361: device buzzard_labels:3V316 -> buzzard_labels:CHG26
- U$362: device buzzard_labels (8):#A112 -> buzzard_labels:PWR27
- U$363: device buzzard_labels (10):3812 -> qwiic#logo#jpg:QWIIC#LOGO#JPG
- U$365: device buzzard_labels (11):#A312 -> buzzard_labels:VIN19
- U$366: device buzzard_labels (11):#A321 -> buzzard_labels:RST19
- U$367: device buzzard_labels (11):#A321 -> buzzard_labels:3V316
- U$368: device buzzard_labels (11):ARTEMIS6 -> buzzard_labels:RST1
- U$369: device buzzard_labels (11):MIC0 -> buzzard_labels (10):RX23
- U$37: device buzzard_labels:VIN19 -> buzzard_labels:810
- U$370: device buzzard_labels (11):MISO5 -> buzzard_labels (10):TX22
- U$371: device buzzard_labels (11):MOSI4 -> buzzard_labels:GND17
- U$374: device buzzard_labels (10):#510 -> buzzard_labels:3V316
- U$375, U$79: device buzzard_labels (10):78 -> buzzard_labels (11):ARTEMIS6
- U$376: device buzzard_labels (10):#66 -> buzzard_labels (11):MIC0
- U$377: device buzzard_labels (11):ARTEMIS6 -> buzzard_labels (11):MISO5
- U$378: device buzzard_labels (11):NANO7 -> buzzard_labels (11):MOSI4
- U$379: device buzzard_labels (14):#D190 -> buzzard_labels (11):NANO7
- U$380: device buzzard_labels (16):#25#SDA21 -> buzzard_labels (11):SCK3
- U$381: device buzzard_labels (16):#27#SCL20 -> buzzard_labels (11):ARTEMIS6
- U$382: device buzzard_labels (16):GND2 -> buzzard_labels (11):NANO7
- U$383: device buzzard_labels (17):____GND____2 -> buzzard_labels (16):GND2
- U$384: device SparkFun-Aesthetics:PRODUCTION_INSTRUCTIONS -> buzzard_labels (17):____GND____2
- U$4: device buzzard_labels:ON1 -> buzzard_labels (7):I#O3
- U$40: device buzzard_labels:RST19 -> buzzard_labels:A10
- U$41: device buzzard_labels:3V316 -> buzzard_labels:A21
- U$42: device buzzard_labels:RST1 -> buzzard_labels:A32
- U$43: device buzzard_labels:ON1 -> buzzard_labels:GND17
- U$44: device buzzard_labels:OFF2 -> buzzard_labels:CHG26
- U$45: device buzzard_labels (8):#A112 -> buzzard_labels (1):90
- U$46: device buzzard_labels (10):#39#TX13 -> buzzard_labels (1):101
- U$47: device buzzard_labels (10):#42#SCL314 -> buzzard_labels (1):112
- U$48: device buzzard_labels (10):#39#TX13 -> buzzard_labels (1):A167
- U$50: device buzzard_labels (8):#A112 -> buzzard_labels (3):RX10
- U$52: device buzzard_labels (10):#43#SDA316 -> buzzard_labels (1):123
- U$53: device buzzard_labels (10):#66 -> buzzard_labels (1):134
- U$54: device buzzard_labels (10):#394 -> buzzard_labels (1):A145
- U$55: device buzzard_labels (10):#510 -> buzzard_labels (1):A156
- U$56: device buzzard_labels (10):#1818 -> buzzard_labels (1):A167
- U$57: device buzzard_labels (10):#42#SCL314 -> buzzard_labels (5):17#SDA21
- U$58: device buzzard_labels:OFF2 -> buzzard_labels:PWR27
- U$59: device buzzard_labels (8):#A112 -> buzzard_labels (2):TX12
- U$60: device buzzard_labels (10):#43#SDA316 -> buzzard_labels (5):18#SCL20
- U$61: device buzzard_labels (10):#66 -> qwiic#logo#jpg:QWIIC#LOGO#JPG
- U$62: device buzzard_labels (10):#394 -> buzzard_labels:GND17
- U$63: device buzzard_labels (10):#510 -> buzzard_labels:VIN19
- U$64: device buzzard_labels (10):#1818 -> buzzard_labels:RST19
- U$65: device buzzard_labels (10):#1818 -> buzzard_labels:3V316
- U$66: device buzzard_labels (10):#4213 -> buzzard_labels:RST1
- U$67: device buzzard_labels (10):#4315 -> buzzard_labels (10):RX23
- U$68: device buzzard_labels (10):#A120 -> buzzard_labels (10):TX22
- U$69: device buzzard_labels (10):#A320 -> buzzard_labels:GND17
- U$70: device buzzard_labels (10):#A320 -> buzzard_labels:RST19
- U$71: device buzzard_labels (10):#A351 -> buzzard_labels:VIN19
- U$72: device buzzard_labels (10):#A351 -> buzzard_labels:3V316
- U$73: device buzzard_labels (10):#A1321 -> buzzard_labels (11):ARTEMIS6
- U$74: device buzzard_labels (10):#A1321 -> buzzard_labels (11):MIC0
- U$75: device buzzard_labels (10):#A2919 -> buzzard_labels (11):MISO5
- U$76: device buzzard_labels (10):#A2919 -> buzzard_labels (11):MOSI4
- U$77: device buzzard_labels (10):#1818 -> buzzard_labels (11):NANO7
- U$78: device buzzard_labels (10):40#RX12 -> buzzard_labels (11):SCK3
- U$80: device buzzard_labels (10):405 -> buzzard_labels (11):NANO7
- U$81: device buzzard_labels (10):3812 -> buzzard_labels (16):GND2
- U$82: device buzzard_labels (10):#4213 -> buzzard_labels (17):____GND____2
- U$83: device buzzard_labels (10):#4315 -> SparkFun-Aesthetics:PRODUCTION_INSTRUCTIONS
- U$84: device buzzard_labels (10):#A120 -> buzzard_labels (16):A00
- U$87: device buzzard_labels (10):#A320 -> buzzard_labels:46
- U$88: device buzzard_labels (10):#A320 -> buzzard_labels:68
- U$89: device buzzard_labels (10):#A351 -> buzzard_labels:79
- U$90: device buzzard_labels (10):#A351 -> buzzard_labels:810
- U$91: device buzzard_labels (10):#A1321 -> buzzard_labels:A10
- U$94: device buzzard_labels (10):#A2919 -> buzzard_labels (1):90
- U$95: device buzzard_labels (10):40#RX12 -> buzzard_labels (1):101
- U$96: device buzzard_labels (10):78 -> buzzard_labels (1):112
- U$97: device buzzard_labels (10):405 -> buzzard_labels (1):123
- U$98: device buzzard_labels (10):3812 -> buzzard_labels (1):134
- U$99: device buzzard_labels (10):RX23 -> buzzard_labels (1):A145
- U1: value MCP73831 -> ARTEMIS_MODULESMD; device SparkFun-IC-Power:SOT23-5 -> Testing:ARTEMIS_FP
- U4: value ARTEMIS_MODULESMD -> MCP73831; device Testing:ARTEMIS_FP -> SparkFun-IC-Power:SOT23-5
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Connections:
- removed net D1: J15.1, U7.D38
- removed net D2: J26.1, U11.D38
- removed net D3: J37.1, U15.D38
- removed net D38: J7.1, U4.D38
- removed net D4: J48.1, U19.D38
- removed net D40/RX1: J2.2, U4.D40
- removed net D40/RX2: J6.2, U7.D40
- removed net D40/RX3: J24.2, U11.D40
- removed net D40/RX4: J35.2, U15.D40
- removed net D40/RX5: J46.2, U19.D40
- removed net D40/RX6: J57.2, U23.D40
- removed net D5: J59.1, U23.D38
- removed net D7/MOSI: J2.4, U4.D7
- removed net D7/MOSI1: J6.4, U7.D7
- removed net D7/MOSI2: J24.4, U11.D7
- removed net D7/MOSI3: J35.4, U15.D7
- removed net D7/MOSI4: J46.4, U19.D7
- removed net D7/MOSI5: J57.4, U23.D7
- removed net N$15 (its old number): R7.1, U1.1
- removed net N$24 (its old number): D17.C, R26.2
- removed net N$25 (its old number): R26.1, U9.1
- removed net N$33 (its old number): R36.2, U13.5
- removed net N$34 (its old number): D24.C, R37.2
- removed net N$42 (its old number): D30.A, R46.1
- removed net N$43 (its old number): R47.2, U17.5
- removed net N$51 (its old number): D36.A, R56.1
- removed net N$52 (its old number): D37.A, R57.1
- removed net ~AD1: J15.6, U7.~AD29
- removed net ~AD10: J24.6, U11.~AD35
- removed net ~AD11: J7.7, U4.~AD11
- removed net ~AD12: J2.8, U4.~AD12
- removed net ~AD13: J5.2, U4.~AD13
- removed net ~AD14: J24.7, U11.~AD32
- removed net ~AD15: J24.8, U11.~AD12
- removed net ~AD16: J25.2, U11.~AD13
- removed net ~AD17: J26.4, U11.~AD31
- removed net ~AD18: J37.6, U15.~AD29
- removed net ~AD19: J37.7, U15.~AD11
- removed net ~AD2: J15.7, U7.~AD11
- removed net ~AD20: J35.6, U15.~AD35
- removed net ~AD21: J35.7, U15.~AD32
- removed net ~AD22: J35.8, U15.~AD12
- removed net ~AD23: J36.2, U15.~AD13
- removed net ~AD24: J37.4, U15.~AD31
- removed net ~AD25: J48.6, U19.~AD29
- removed net ~AD26: J48.7, U19.~AD11
- removed net ~AD27: J46.6, U19.~AD35
- removed net ~AD28: J46.7, U19.~AD32
- removed net ~AD29: J7.6, U4.~AD29
- removed net ~AD3: J6.6, U7.~AD35
- removed net ~AD3/SWO: J11.6, J5.1, U4.~AD33/SWO
- removed net ~AD3/SWO1: J22.6, J8.1, U7.~AD33/SWO
- removed net ~AD3/SWO2: J25.1, J33.6, U11.~AD33/SWO
- removed net ~AD3/SWO3: J36.1, J44.6, U15.~AD33/SWO
- removed net ~AD3/SWO4: J47.1, J55.6, U19.~AD33/SWO
- removed net ~AD3/SWO5: J58.1, J66.6, U23.~AD33/SWO
- removed net ~AD30: J46.8, U19.~AD12
- removed net ~AD31: J7.4, U4.~AD31
- removed net ~AD32: J2.7, U4.~AD32
- removed net ~AD33: J47.2, U19.~AD13
- removed net ~AD34: J48.4, U19.~AD31
- removed net ~AD35: J2.6, U4.~AD35
- removed net ~AD36: J59.6, U23.~AD29
- removed net ~AD37: J59.7, U23.~AD11
- removed net ~AD38: J57.6, U23.~AD35
- removed net ~AD39: J57.7, U23.~AD32
- removed net ~AD4: J6.7, U7.~AD32
- removed net ~AD40: J57.8, U23.~AD12
- removed net ~AD41: J58.2, U23.~AD13
- removed net ~AD42: J59.4, U23.~AD31
- removed net ~AD5: J6.8, U7.~AD12
- removed net ~AD6: J8.2, U7.~AD13
- removed net ~AD7: J15.4, U7.~AD31
- removed net ~AD8: J26.6, U11.~AD29
- removed net ~AD9: J26.7, U11.~AD11
- removed net ~D16: J37.5, U15.~D18
- removed net ~D17: U19.~D4
- removed net ~D18: J7.5, U4.~D18
- removed net ~D19: U19.~D22
- removed net ~D20: J48.2, U19.~D42
- removed net ~D21: J48.3, U19.~D43
- removed net ~D23: J48.5, U19.~D18
- removed net ~D24: U23.~D4
- removed net ~D25: U23.~D22
- removed net ~D26: J59.2, U23.~D42
- removed net ~D27: J59.3, U23.~D43
- removed net ~D28: J59.5, U23.~D18
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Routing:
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- added copper zone on layer 15, net 3.3V6
- added copper zone on layer 15, net 3.3V7
- added copper zone on layer 1, net GND6
- added copper zone on layer 16, net GND6
- added copper zone on layer 2, net GND6
- added copper zone on layer 1, net GND7
- added copper zone on layer 16, net GND7
- added copper zone on layer 2, net GND7
- added copper zone on layer 1, net SHLD6
- added copper zone on layer 16, net SHLD6
- added copper zone on layer 1, net SHLD7
- added copper zone on layer 16, net SHLD7
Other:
- board size 120.7 x 75.7 mm -> 120.7 x 96.5 mm
- board text added: "x02"
- board text removed: "v10"
